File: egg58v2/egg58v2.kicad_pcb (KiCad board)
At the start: 2 copper layers, 141.1 x 125.8 mm, 34 parts, among them J1 AudioJack4, SW11 SW_PUSH_LED, SW12 SW_PUSH_LED, SW13 SW_PUSH_LED, SW14 SW_PUSH_LED, SW15 SW_PUSH_LED, SW16 SW_PUSH_LED, SW21 SW_PUSH_LED, SW22 SW_PUSH_LED, SW23 SW_PUSH_LED, SW24 SW_PUSH_LED, SW25 SW_PUSH_LED, SW26 SW_PUSH_LED, SW31 SW_PUSH_LED, SW32 SW_PUSH_LED, SW33 SW_PUSH_LED, SW34 SW_PUSH_LED, SW35 SW_PUSH_LED, SW36 SW_PUSH_LED, SW41 SW_PUSH_LED, SW42 SW_PUSH_LED, SW43 SW_PUSH_LED, SW44 SW_PUSH_LED, SW45 SW_PUSH_LED, SW46 SW_PUSH_LED, SW52 SW_PUSH_LED, SW53 SW_PUSH_LED, SW54 SW_PUSH_LED, SW55 SW_PUSH_LED, SW56 SW_PUSH_LED, U1 Elite-C

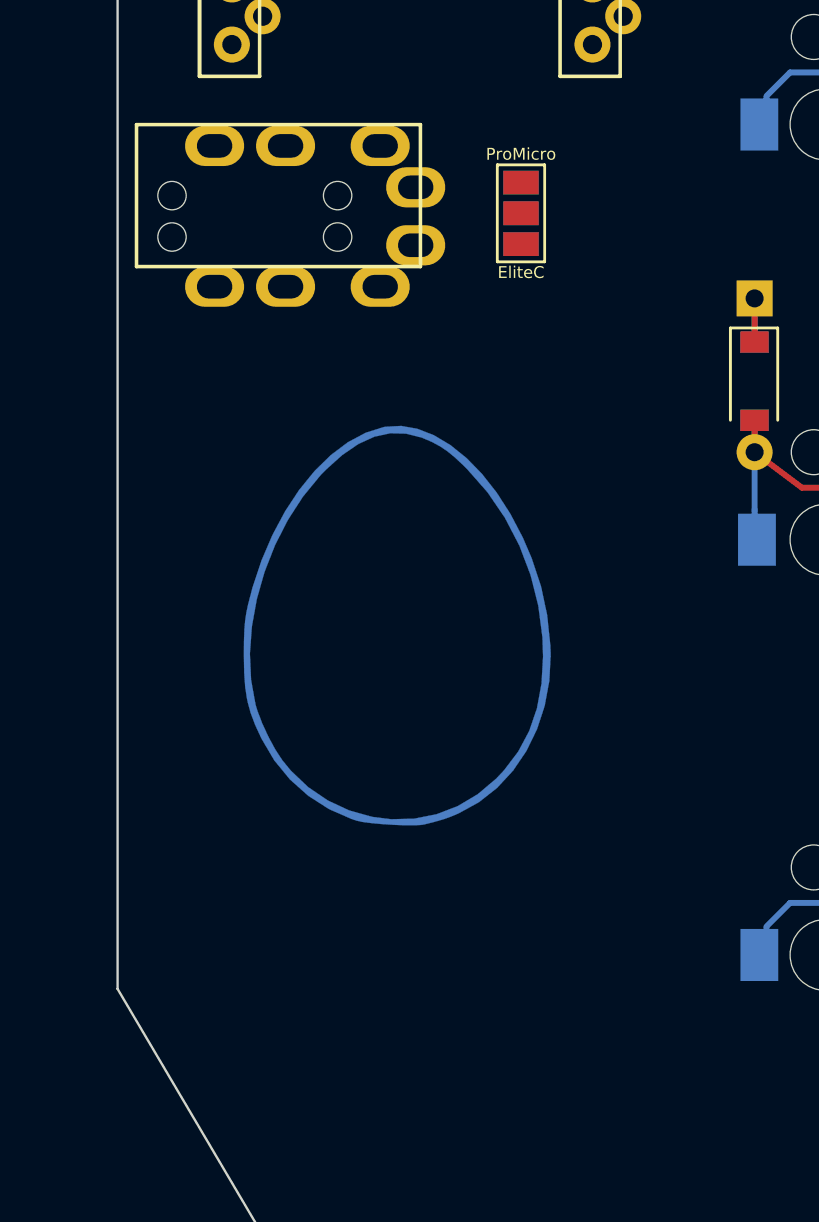
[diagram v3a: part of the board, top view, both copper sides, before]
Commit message: add option for i2c back
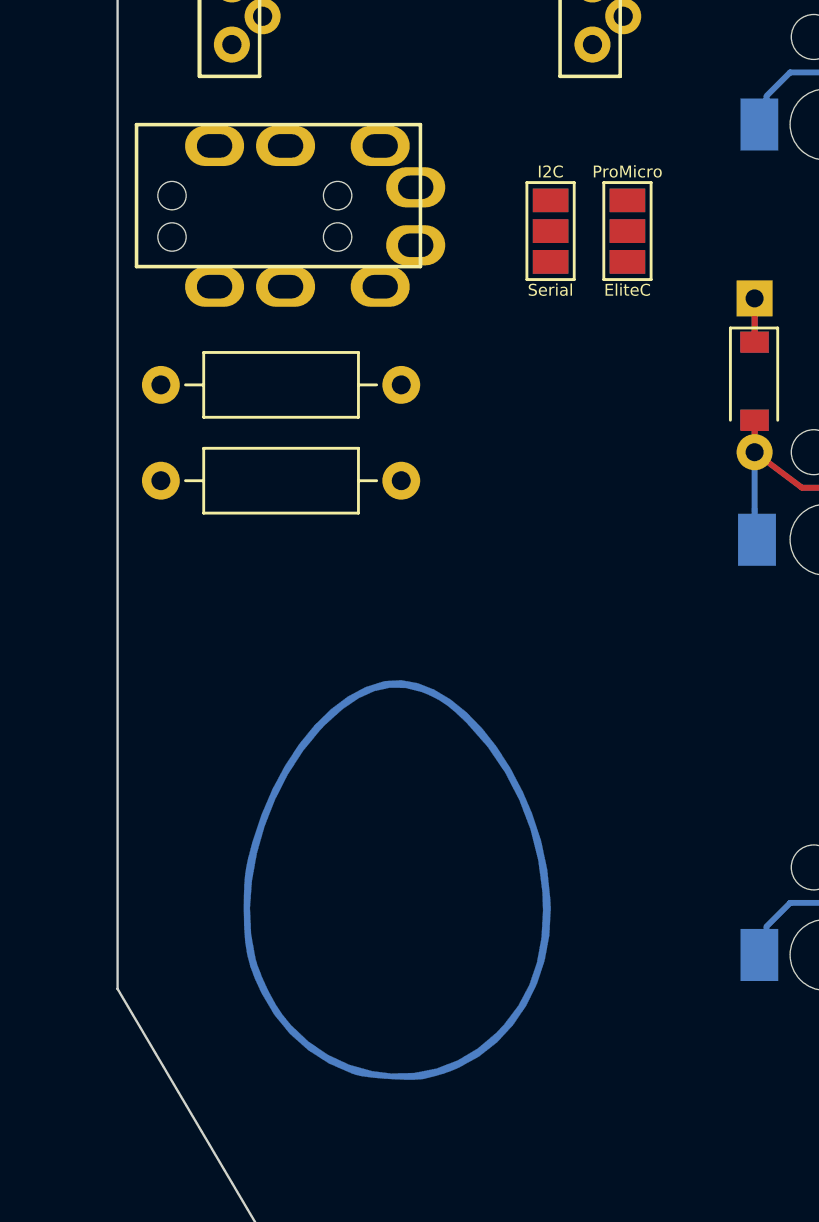
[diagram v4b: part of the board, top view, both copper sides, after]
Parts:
- added JP2: Jumper_NC_Dual, egg58v2:SolderJumper-3_P1.3mm_Open_Pad1.0x1.5mm_NumberLabels, F.Cu at (126.2, 81.0)
- added R1: 100k, egg58v2:R_Axial_DIN0207_L6.3mm_D2.5mm_P10.16mm_Horizontal, F.Cu at (119.9, 87.5)
- added R2: 100k, egg58v2:R_Axial_DIN0207_L6.3mm_D2.5mm_P10.16mm_Horizontal, F.Cu at (119.9, 91.5)
- moved G*** 10.8 mm to (119.8, 108.5)
- moved JP1 4.56 mm to (129.5, 81.0)
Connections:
- J1 pad 1: VDD -> VCC
- J1 pad 3: SDA -> DATA
- JP1 pad 2: VDD -> VCC
- JP1 pad 3: VCC -> VREG
- U1 pad 2: Net-(U1-Pad2) -> SERIAL
- U1 pad 21: VCC -> VREG

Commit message: starting routing
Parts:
- moved U1 2.00 mm to (118.5, 58.8)
- moved JP1 1.12 mm to (128.5, 80.5), turned to 90 degrees
- moved JP2 1.12 mm to (125.2, 80.5), turned to 270 degrees
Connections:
- SW11 pad 1: VDD -> VCC
- SW12 pad 1: VDD -> VCC
- SW13 pad 1: VDD -> VCC
- SW14 pad 1: VDD -> VCC
- SW15 pad 1: VDD -> VCC
- SW16 pad 1: VDD -> VCC
- SW21 pad 1: VDD -> VCC
- SW22 pad 1: VDD -> VCC
- SW23 pad 1: VDD -> VCC
- SW24 pad 1: VDD -> VCC
- SW25 pad 1: VDD -> VCC
- SW26 pad 1: VDD -> VCC
- SW31 pad 1: VDD -> VCC
- SW32 pad 1: VDD -> VCC
- SW33 pad 1: VDD -> VCC
- SW34 pad 1: VDD -> VCC
- SW35 pad 1: VDD -> VCC
- SW36 pad 1: VDD -> VCC
- SW41 pad 1: VDD -> VCC
- SW42 pad 1: VDD -> VCC
- SW43 pad 1: VDD -> VCC
- SW44 pad 1: VDD -> VCC
- SW45 pad 1: VDD -> VCC
- SW46 pad 1: VDD -> VCC
- SW52 pad 1: VDD -> VCC
- SW53 pad 1: VDD -> VCC
- SW54 pad 1: VDD -> VCC
- SW55 pad 1: VDD -> VCC
- SW56 pad 1: VDD -> VCC
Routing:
- net SCL: track 0.00 -> 62.8 mm
- net VBUS: track 0.00 -> 58.4 mm, vias 0 -> 1
- net SERIAL: track 0.00 -> 53.7 mm, vias 0 -> 1
- net VREG: track 0.00 -> 47.1 mm, vias 0 -> 1
- net GND: track 0.00 -> 44.4 mm
- net VCC: track 0.00 -> 40.6 mm, vias 0 -> 1
- net SDA: track 0.00 -> 37.1 mm, vias 0 -> 1
- net DATA: track 0.00 -> 24.4 mm, vias 0 -> 1
- net RGB: track 0.00 -> 17.0 mm
- net Net-(U1-Pad20): track 0.00 -> 14.4 mm
- net Net-(U1-Pad22): track 0.00 -> 14.4 mm
- net Net-(U1-Pad19): track 0.00 -> 14.4 mm

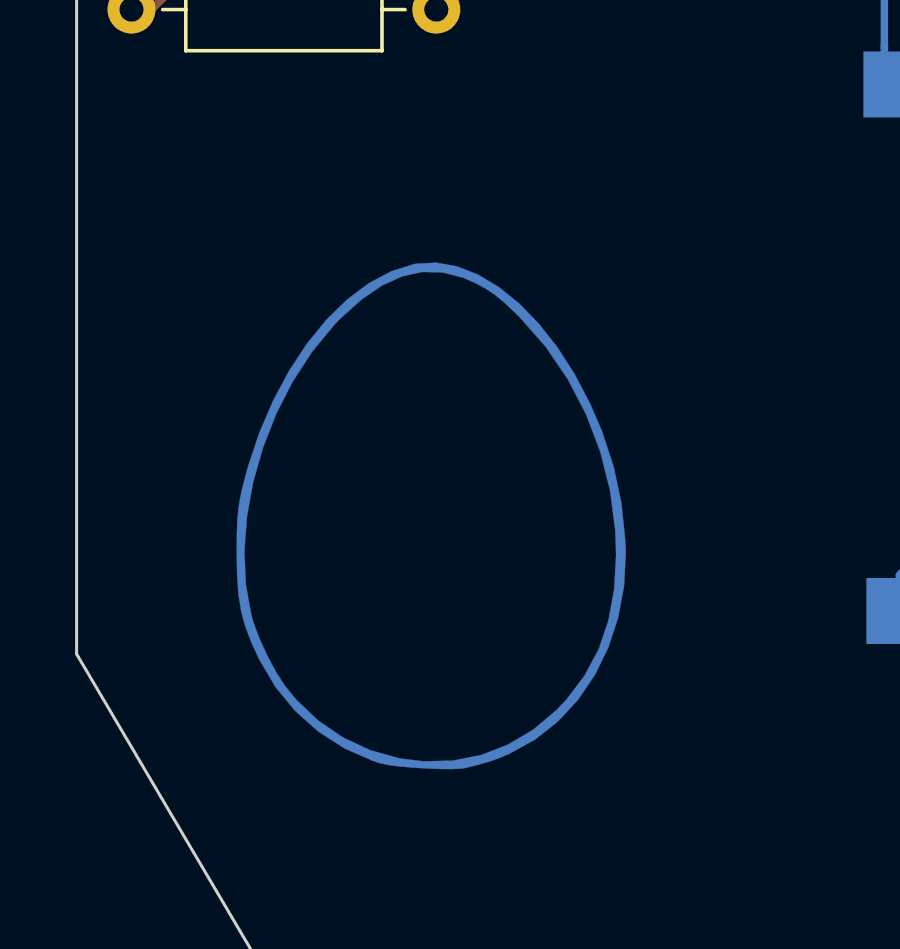
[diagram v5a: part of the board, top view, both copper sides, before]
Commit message: footprint updates
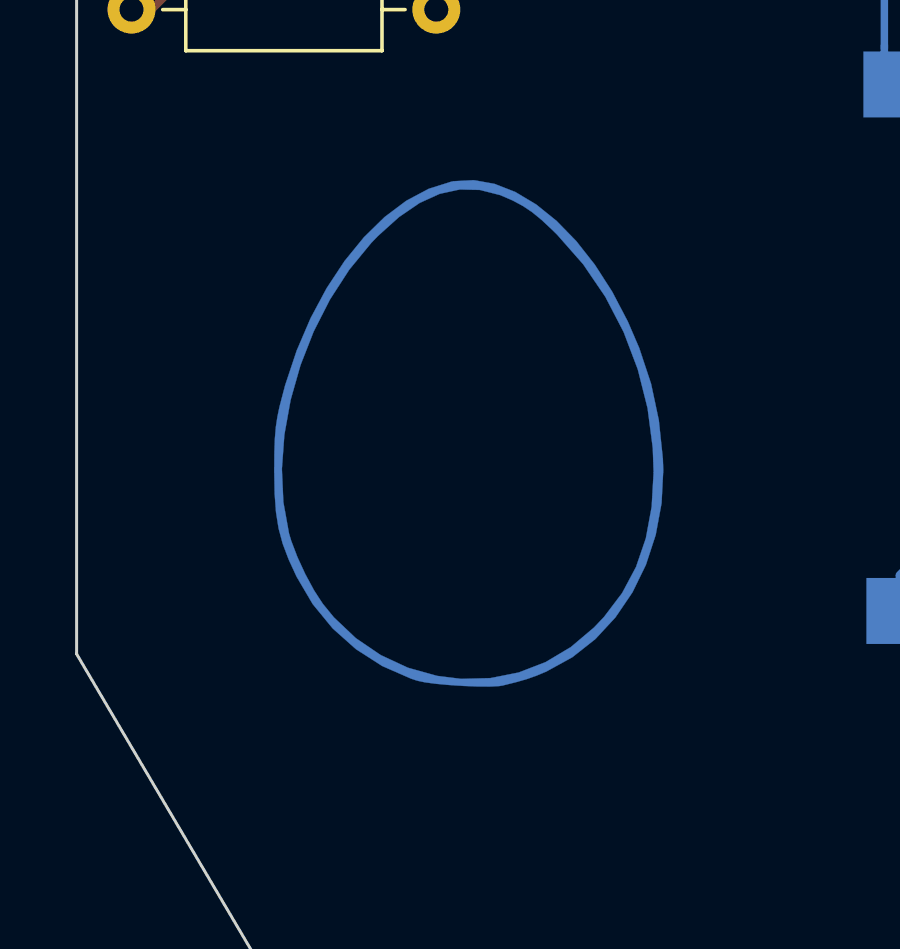
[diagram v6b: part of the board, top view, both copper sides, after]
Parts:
- moved G*** 3.02 mm to (121.0, 105.8)

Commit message: starting routing for matrix
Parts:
- turned JP1 to 270 degrees
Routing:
- net VCC: track 40.6 -> 722.5 mm, vias 1 -> 6
- net Row5: track 0.00 -> 188.6 mm, vias 0 -> 3
- net Row4: track 0.00 -> 178.2 mm, vias 0 -> 3
- net Col1: track 0.00 -> 161.7 mm, vias 0 -> 2
- net Row2: track 0.00 -> 152.1 mm, vias 0 -> 1
- net Row3: track 0.00 -> 145.2 mm, vias 0 -> 2
- net Col2: track 0.00 -> 139.6 mm, vias 0 -> 2
- net Row1: track 0.00 -> 138.2 mm, vias 0 -> 1
- net Col3: track 0.00 -> 123.7 mm, vias 0 -> 2
- net Col4: track 0.00 -> 104.6 mm, vias 0 -> 2
- net Col5: track 0.00 -> 88.2 mm, vias 0 -> 2
- net Col6: track 0.00 -> 71.3 mm
- net GND: track 44.4 -> 5.95 mm
- net SDA: track 37.1 -> 70.4 mm, vias 1 -> 3
- net Net-(U1-Pad7): track 0.00 -> 17.5 mm, vias 0 -> 1
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
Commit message: routing fixes
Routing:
- net Col4: track 104.6 -> 107.5 mm
- net Row2: track 152.1 -> 149.8 mm
- net VCC: track 722.5 -> 724.2 mm
- net Col3: track 123.7 -> 124.5 mm
- net SCL: track 61.1 -> 60.3 mm
- net Col2: track 139.6 -> 140.3 mm
- net SERIAL: track 56.4 -> 57.1 mm
- net Col6: track 71.3 -> 70.7 mm
- net VBUS: track 56.2 -> 56.8 mm
- net Col5: track 88.2 -> 88.7 mm
